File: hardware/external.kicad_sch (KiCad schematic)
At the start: 8 parts

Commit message: Fixed some erros, changed to 3V
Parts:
- renumbered PortA_Ext to PortA_Ext1, PortC_Ext to PortC_Ext1, SPI_EXT_{2} to SPI_EXT_{2}1, SPI_EXT_{3} to SPI_EXT_{3}1, SPI_EXT_{3} to SPI_EXT_{3}2
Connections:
- net SPI_CS_{3}: no longer SPI_EXT_{3}2.12 (Pin_12)
- new net SPI_CS_{4}: SPI_EXT_{3}2.12 (Pin_12)
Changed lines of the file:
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@@
 	(wire
 		(pts
+			(xy 222.25 35.56) (xy 231.14 35.56)
+		)
+		(stroke
+			(width 0)
+			(type default)
+		)
+	)
+	(wire
+		(pts
 			(xy 99.06 87.63) (xy 101.6 87.63)
 		)
@@
 	(wire
 		(pts
-			(xy 231.14 35.56) (xy 222.25 35.56)
+			(xy 137.16 138.43) (xy 129.54 138.43)
 		)
 		(stroke
@@
 	(wire
 		(pts
-			(xy 137.16 138.43) (xy 129.54 138.43)
+			(xy 140.97 95.25) (xy 143.51 95.25)
 		)
 		(stroke
@@
 	(wire
 		(pts
-			(xy 140.97 95.25) (xy 143.51 95.25)
+			(xy 58.42 138.43) (xy 50.8 138.43)
 		)
 		(stroke
@@
 	(wire
 		(pts
-			(xy 58.42 138.43) (xy 50.8 138.43)
+			(xy 99.06 90.17) (xy 101.6 90.17)
 		)
 		(stroke
@@
 	(wire
 		(pts
-			(xy 99.06 90.17) (xy 101.6 90.17)
+			(xy 222.25 40.64) (xy 231.14 40.64)
 		)
 		(stroke
@@
 		)
 	)
-	(bus
+	(wire
 		(pts
-			(xy 48.26 128.27) (xy 48.26 130.81)
+			(xy 222.25 38.1) (xy 231.14 38.1)
 		)
 		(stroke
@@
 		)
 	)
-	(wire
+	(bus
 		(pts
-			(xy 231.14 38.1) (xy 222.25 38.1)
+			(xy 48.26 128.27) (xy 48.26 130.81)
 		)
 		(stroke
@@
 	(wire
 		(pts
+			(xy 222.25 33.02) (xy 231.14 33.02)
+		)
+		(stroke
+			(width 0)
+			(type default)
+		)
+	)
+	(wire
+		(pts
 			(xy 140.97 80.01) (xy 143.51 80.01)
 		)
@@
 	(wire
 		(pts
-			(xy 118.11 33.02) (xy 120.65 33.02)
+			(xy 222.25 25.4) (xy 231.14 25.4)
 		)
 		(stroke
@@
 		)
 	)
-	(bus
+	(wire
 		(pts
-			(xy 64.77 50.8) (xy 64.77 58.42)
+			(xy 118.11 33.02) (xy 120.65 33.02)
 		)
 		(stroke
@@
 	(wire
 		(pts
-			(xy 231.14 33.02) (xy 222.25 33.02)
-		)
-		(stroke
-			(width 0)
-			(type default)
-		)
-	)
-	(wire
-		(pts
 			(xy 91.44 35.56) (xy 95.25 35.56)
 		)
@@
 		)
 	)
+	(wire
+		(pts
+			(xy 222.25 27.94) (xy 231.14 27.94)
+		)
+		(stroke
+			(width 0)
+			(type default)
+		)
+	)
 	(bus
 		(pts
@@
 	(wire
 		(pts
-			(xy 58.42 135.89) (xy 50.8 135.89)
+			(xy 222.25 30.48) (xy 231.14 30.48)
 		)
 		(stroke
@@
 		)
 	)
-	(bus
+	(wire
 		(pts
-			(xy 87.63 133.35) (xy 87.63 135.89)
+			(xy 58.42 135.89) (xy 50.8 135.89)
 		)
 		(stroke
@@
 	(bus
 		(pts
-			(xy 106.68 50.8) (xy 106.68 57.15)
+			(xy 87.63 133.35) (xy 87.63 135.89)
 		)
 		(stroke
@@
 		)
 	)
-	(wire
-		(pts
-			(xy 231.14 40.64) (xy 222.25 40.64)
-		)
-		(stroke
-			(width 0)
-			(type default)
-		)
-	)
 	(bus
 		(pts
@@
 		)
 	)
-	(bus
-		(pts
-			(xy 148.59 50.8) (xy 148.59 57.15)
-		)
-		(stroke
-			(width 0)
-			(type default)
-		)
-	)
 	(wire
 		(pts
@@
 	(wire
 		(pts
-			(xy 231.14 43.18) (xy 222.25 43.18)
-		)
-		(stroke
-			(width 0)
-			(type default)
-		)
-	)
-	(wire
-		(pts
 			(xy 118.11 43.18) (xy 120.65 43.18)
 		)
@@
 		)
 	)
-	(wire
-		(pts
-			(xy 231.14 25.4) (xy 222.25 25.4)
-		)
-		(stroke
-			(width 0)
-			(type default)
-		)
-	)
 	(bus
 		(pts
@@
 	(wire
 		(pts
-			(xy 231.14 30.48) (xy 222.25 30.48)
+			(xy 76.2 43.18) (xy 78.74 43.18)
 		)
 		(stroke
@@
 	(wire
 		(pts
-			(xy 76.2 43.18) (xy 78.74 43.18)
+			(xy 57.15 82.55) (xy 59.69 82.55)
 		)
 		(stroke
@@
 	(wire
 		(pts
-			(xy 57.15 82.55) (xy 59.69 82.55)
+			(xy 222.25 43.18) (xy 231.14 43.18)
 		)
 		(stroke
@@
 		)
 	)
-	(wire
-		(pts
-			(xy 231.14 27.94) (xy 222.25 27.94)
-		)
-		(stroke
-			(width 0)
-			(type default)
-		)
-	)
 	(bus
 		(pts
@@
 	)
 	(label "D2"
-		(at 227.33 38.1 180)
+		(at 231.14 38.1 180)
 		(effects
 			(font
@@
 	)
 	(label "D0"
-		(at 227.33 43.18 180)
+		(at 231.14 43.18 180)
 		(effects
 			(font
@@
 	)
 	(label "D5"
-		(at 227.33 30.48 180)
+		(at 231.14 30.48 180)
 		(effects
 			(font
@@
 	)
 	(label "D3"
-		(at 227.33 35.56 180)
+		(at 231.14 35.56 180)
 		(effects
 			(font
@@
 	)
 	(label "D1"
-		(at 227.33 40.64 180)
+		(at 231.14 40.64 180)
 		(effects
 			(font
@@
 	)
 	(label "D6"
-		(at 227.33 27.94 180)
+		(at 231.14 27.94 180)
 		(effects
 			(font
@@
 	)
 	(label "D7"
-		(at 227.33 25.4 180)
+		(at 231.14 25.4 180)
 		(effects
 			(font
@@
 	)
 	(label "D4"
-		(at 227.33 33.02 180)
+		(at 231.14 33.02 180)
 		(effects
 			(font
@@
 		)
 	)
-	(global_label "SPI_CS_{3}"
+	(global_label "SPI_CS_{4}"
 		(shape input)
 		(at 158.75 92.71 0)
@@
 		(dnp no)
 		(fields_autoplaced yes)
-		(property "Reference" "SPI_EXT_{2}"
+		(property "Reference" "SPI_EXT_{2}1"
 			(at 66.04 73.66 0)
 			(effects
@@
 			(project "Lambda One"
 				(path "/73ea9964-373f-4fdc-b03e-f532cf836c0d/8596ee45-8820-47ce-a360-877e286ae437"
-					(reference "SPI_EXT_{2}")
+					(reference "SPI_EXT_{2}1")
 					(unit 1)
 				)
@@
 		(dnp no)
 		(fields_autoplaced yes)
-		(property "Reference" "SPI_EXT_{3}"
+		(property "Reference" "SPI_EXT_{3}2"
 			(at 149.86 73.66 0)
 			(effects
@@
 			(project "Lambda One"
 				(path "/73ea9964-373f-4fdc-b03e-f532cf836c0d/8596ee45-8820-47ce-a360-877e286ae437"
-					(reference "SPI_EXT_{3}")
+					(reference "SPI_EXT_{3}2")
 					(unit 1)
 				)
@@
 		(dnp no)
 		(fields_autoplaced yes)
-		(property "Reference" "PortC_Ext"
+		(property "Reference" "PortC_Ext1"
 			(at 105.41 138.4299 0)
 			(effects
@@
 			(project "Lambda One"
 				(path "/73ea9964-373f-4fdc-b03e-f532cf836c0d/8596ee45-8820-47ce-a360-877e286ae437"
-					(reference "PortC_Ext")
+					(reference "PortC_Ext1")
 					(unit 1)
 				)
@@
 		(dnp no)
 		(fields_autoplaced yes)
-		(property "Reference" "PortA_Ext"
+		(property "Reference" "PortA_Ext1"
 			(at 66.04 138.4299 0)
 			(effects
@@
 			(project "Lambda One"
 				(path "/73ea9964-373f-4fdc-b03e-f532cf836c0d/8596ee45-8820-47ce-a360-877e286ae437"
-					(reference "PortA_Ext")
+					(reference "PortA_Ext1")
 					(unit 1)
 				)
@@
 		(dnp no)
 		(fields_autoplaced yes)
-		(property "Reference" "SPI_EXT_{3}"
+		(property "Reference" "SPI_EXT_{3}1"
 			(at 107.95 73.66 0)
 			(effects
@@
 			(project "Lambda One"
 				(path "/73ea9964-373f-4fdc-b03e-f532cf836c0d/8596ee45-8820-47ce-a360-877e286ae437"
-					(reference "SPI_EXT_{3}")
+					(reference "SPI_EXT_{3}1")
 					(unit 1)
 				)

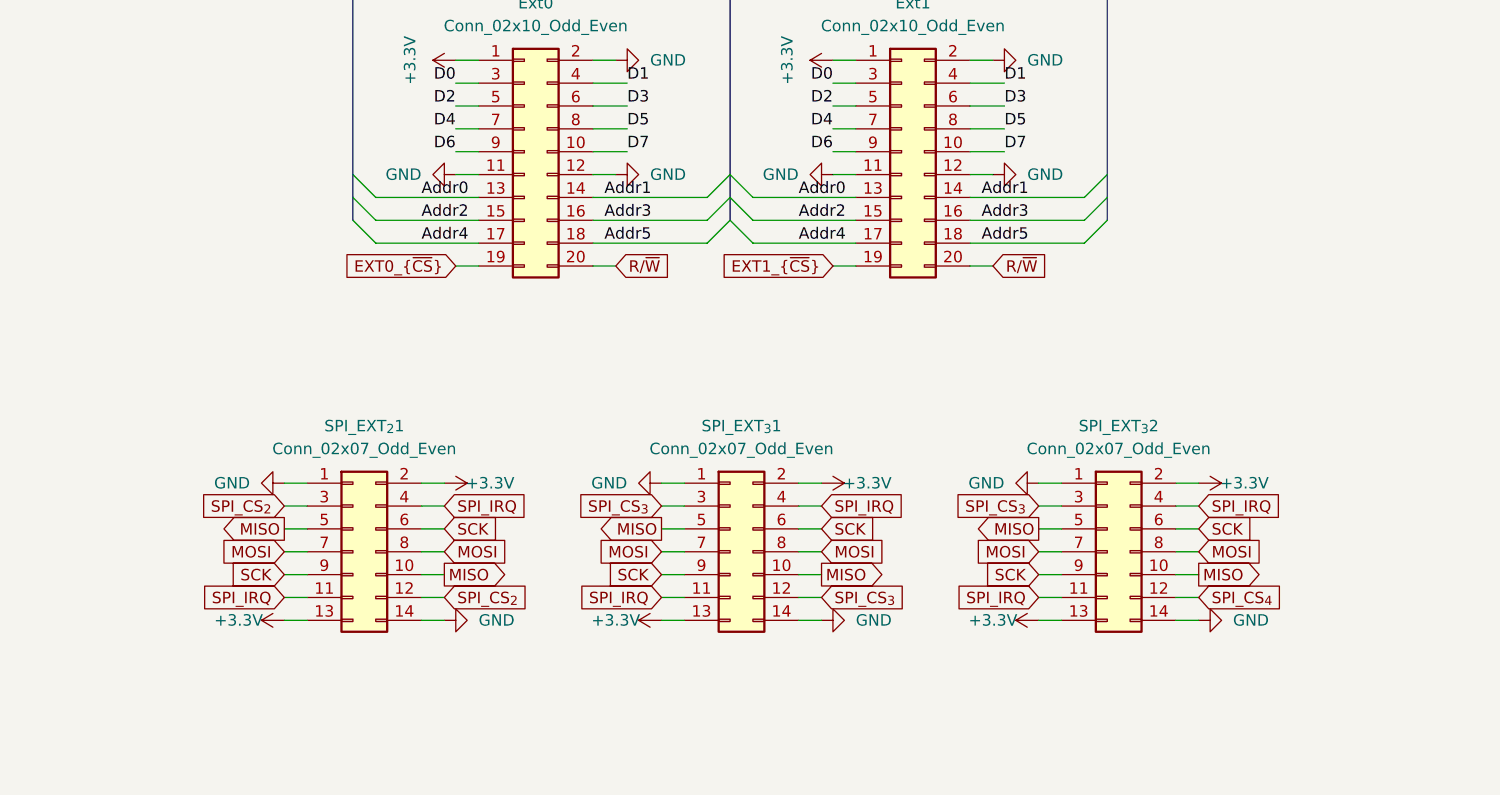
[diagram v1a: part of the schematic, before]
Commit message: Fixed critical bugs on the system related to memory maping and IC selections
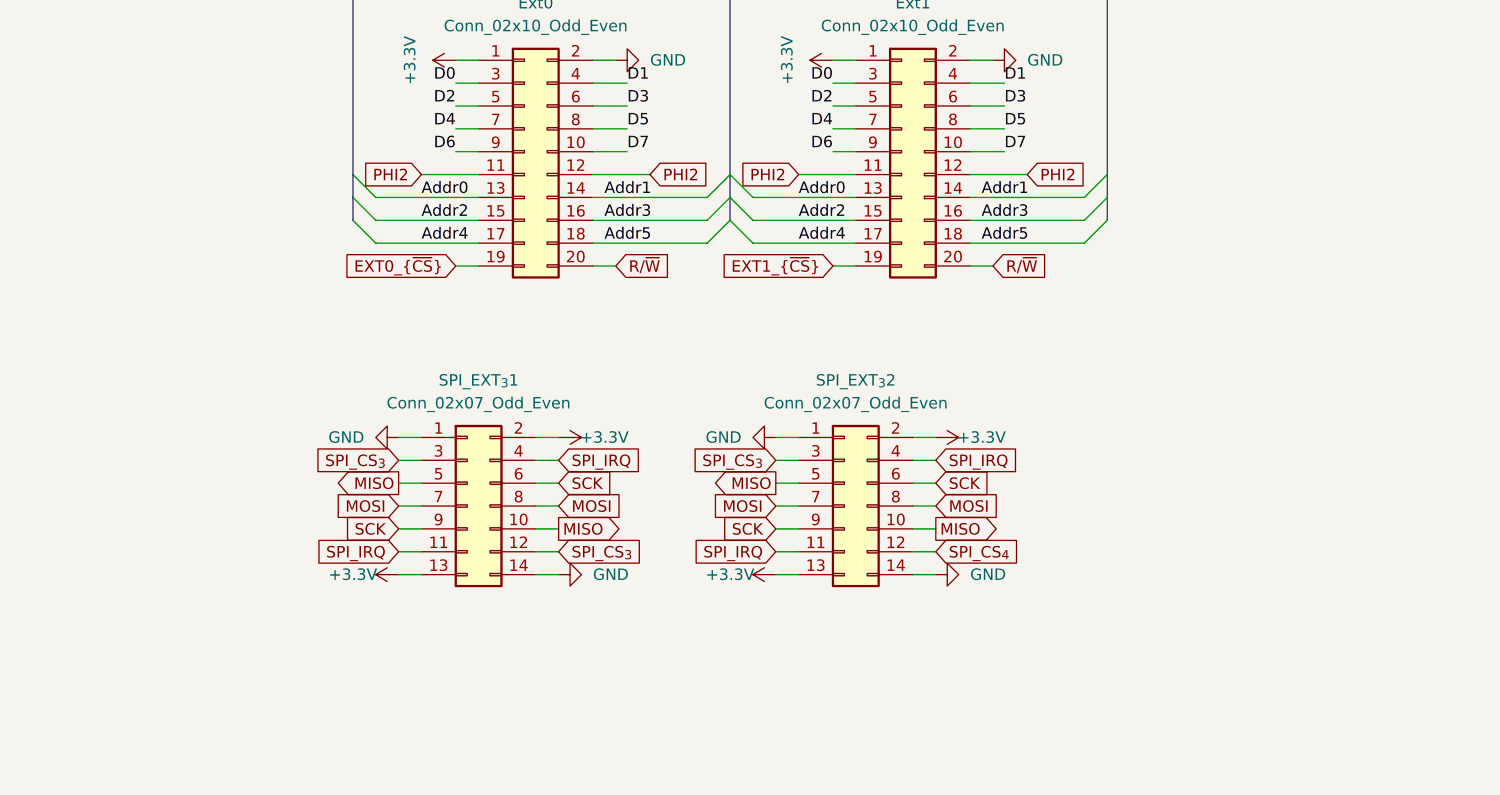
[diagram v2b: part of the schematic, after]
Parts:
- removed SPI_EXT_{2}1: Conn_02x07_Odd_Even, Connector_PinSocket_2.54mm:PinSocket_2x07_P2.54mm_Vertical, symbol Connector_Generic:Conn_02x07_Odd_Even
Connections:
- net GND: no longer Ext0.11 (Pin_11), Ext0.12 (Pin_12), Ext1.11 (Pin_11), Ext1.12 (Pin_12)
- new net PHI2: Ext0.11 (Pin_11), Ext0.12 (Pin_12), Ext1.11 (Pin_11), Ext1.12 (Pin_12)
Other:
- moved on the sheet: SPI_EXT_{3}1, SPI_EXT_{3}2

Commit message: Fixes and addres fix adding VDA AND VPA
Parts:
- added J4: Conn_02x04_Odd_Even, Connector_PinHeader_2.54mm:PinHeader_2x04_P2.54mm_Vertical, symbol Connector_Generic:Conn_02x04_Odd_Even
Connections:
- net +3.3V: now also J4.1 (Pin_1), J4.3 (Pin_3), J4.5 (Pin_5), J4.7 (Pin_7)
- net GND: now also J4.2 (Pin_2), J4.4 (Pin_4), J4.6 (Pin_6), J4.8 (Pin_8)
- net PHI2 renamed CLK
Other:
- moved on the sheet: SPI_EXT_{3}2

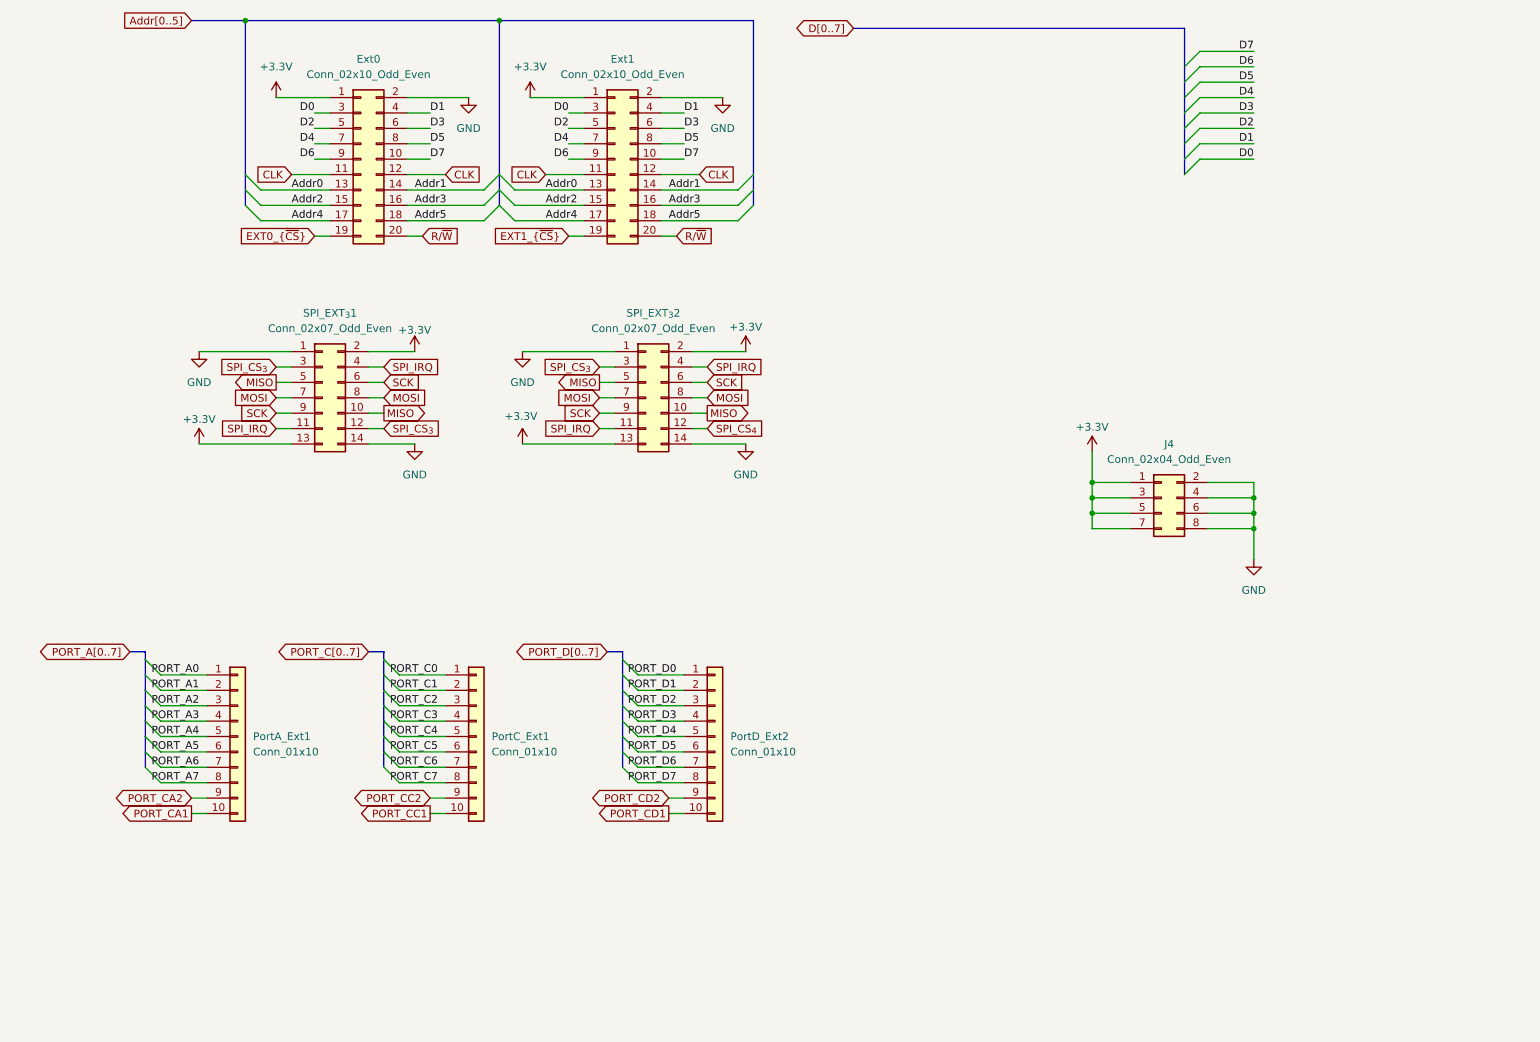
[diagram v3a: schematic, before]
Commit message: IMproved Serial With New CHIP, IMproved Video, Added external Serial Connections
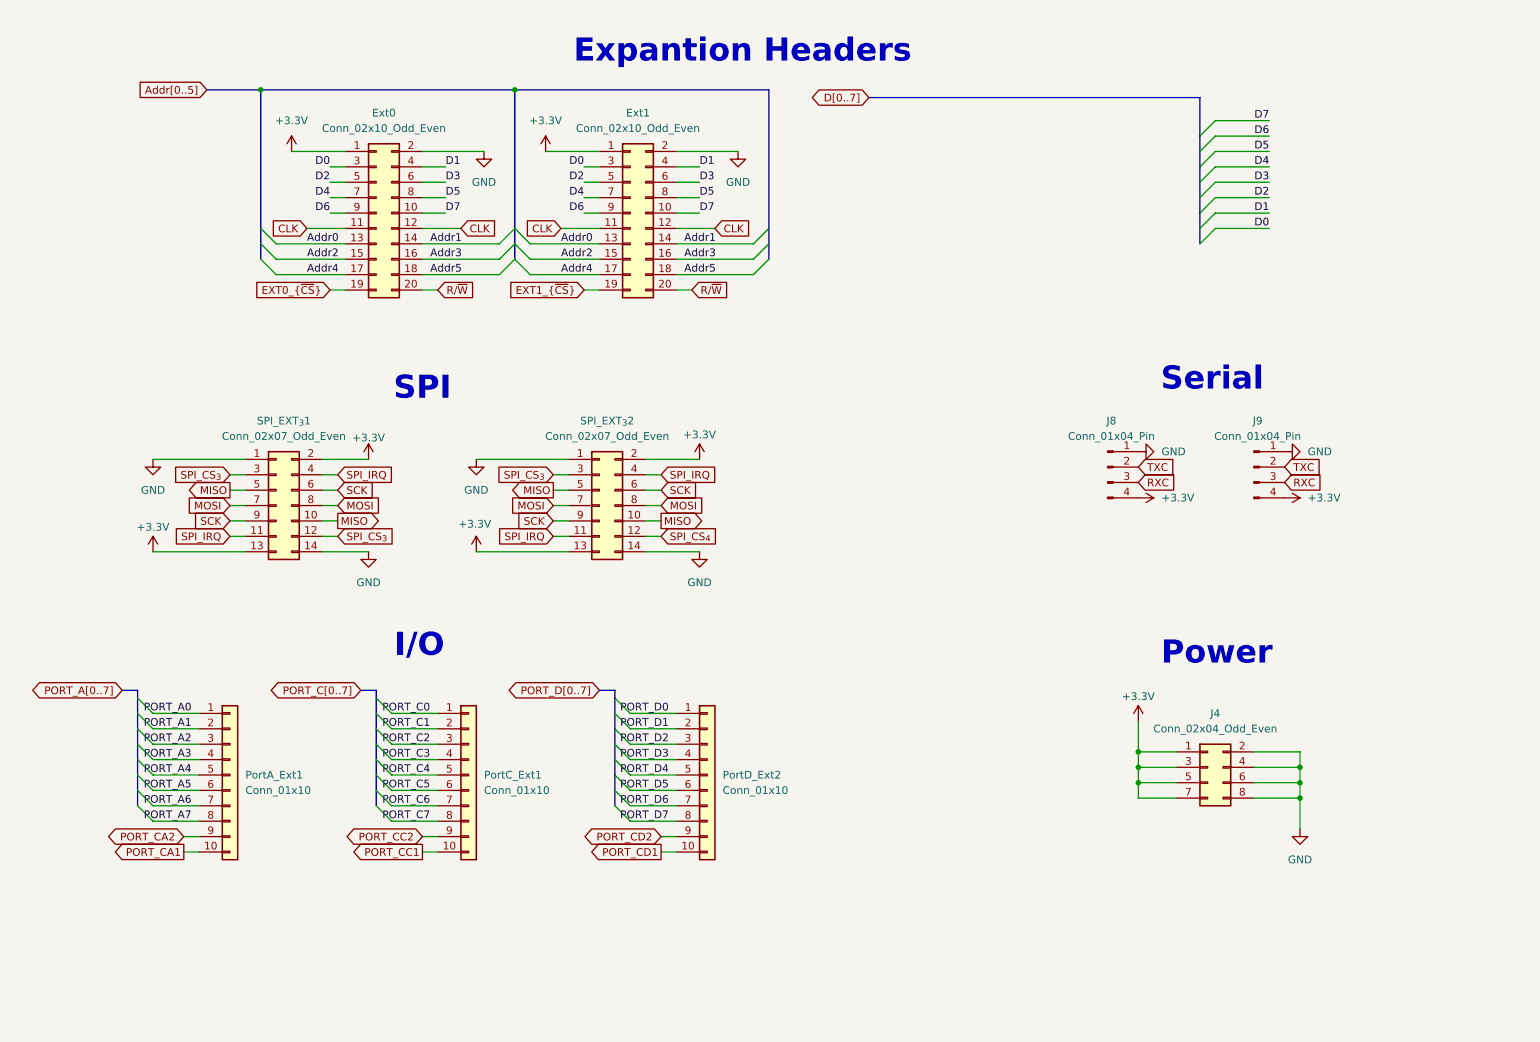
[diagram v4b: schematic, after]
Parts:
- added J8, J9: Conn_01x04_Pin, Connector_PinHeader_2.54mm:PinHeader_1x04_P2.54mm_Vertical, symbol Connector:Conn_01x04_Pin
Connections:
- net +3.3V: now also J8.4 (Pin_4), J9.4 (Pin_4)
- net GND: now also J8.1 (Pin_1), J9.1 (Pin_1)
- new net RXC: J8.3 (Pin_3), J9.3 (Pin_3)
- new net TXC: J8.2 (Pin_2), J9.2 (Pin_2)
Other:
- note added: "Expantion Headers"
- note added: "I/O"
- note added: "Power"
- note added: "SPI"
- note added: "Serial"
- moved on the sheet: Ext0, Ext1, J4, PortA_Ext1, PortC_Ext1, PortD_Ext2, SPI_EXT_{3}1, SPI_EXT_{3}2

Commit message: Minor Improvemnts
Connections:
- net RXC: no longer J9.3 (Pin_3)
- net TXC: no longer J9.2 (Pin_2)
- new net RXD: J9.3 (Pin_3)
- new net TXD: J9.2 (Pin_2)
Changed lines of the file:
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@@
 		)
 	)
-	(global_label "TXC"
+	(global_label "TXD"
 		(shape input)
 		(at 236.22 93.98 0)
@@
 		)
 	)
-	(global_label "RXC"
+	(global_label "RXD"
 		(shape input)
 		(at 236.22 96.52 0)
